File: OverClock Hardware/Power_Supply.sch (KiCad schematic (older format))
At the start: 29 parts, among them J1 USB_C_Plug, U1 AP7365, U2 TLV62569, U3 10M02SCE144

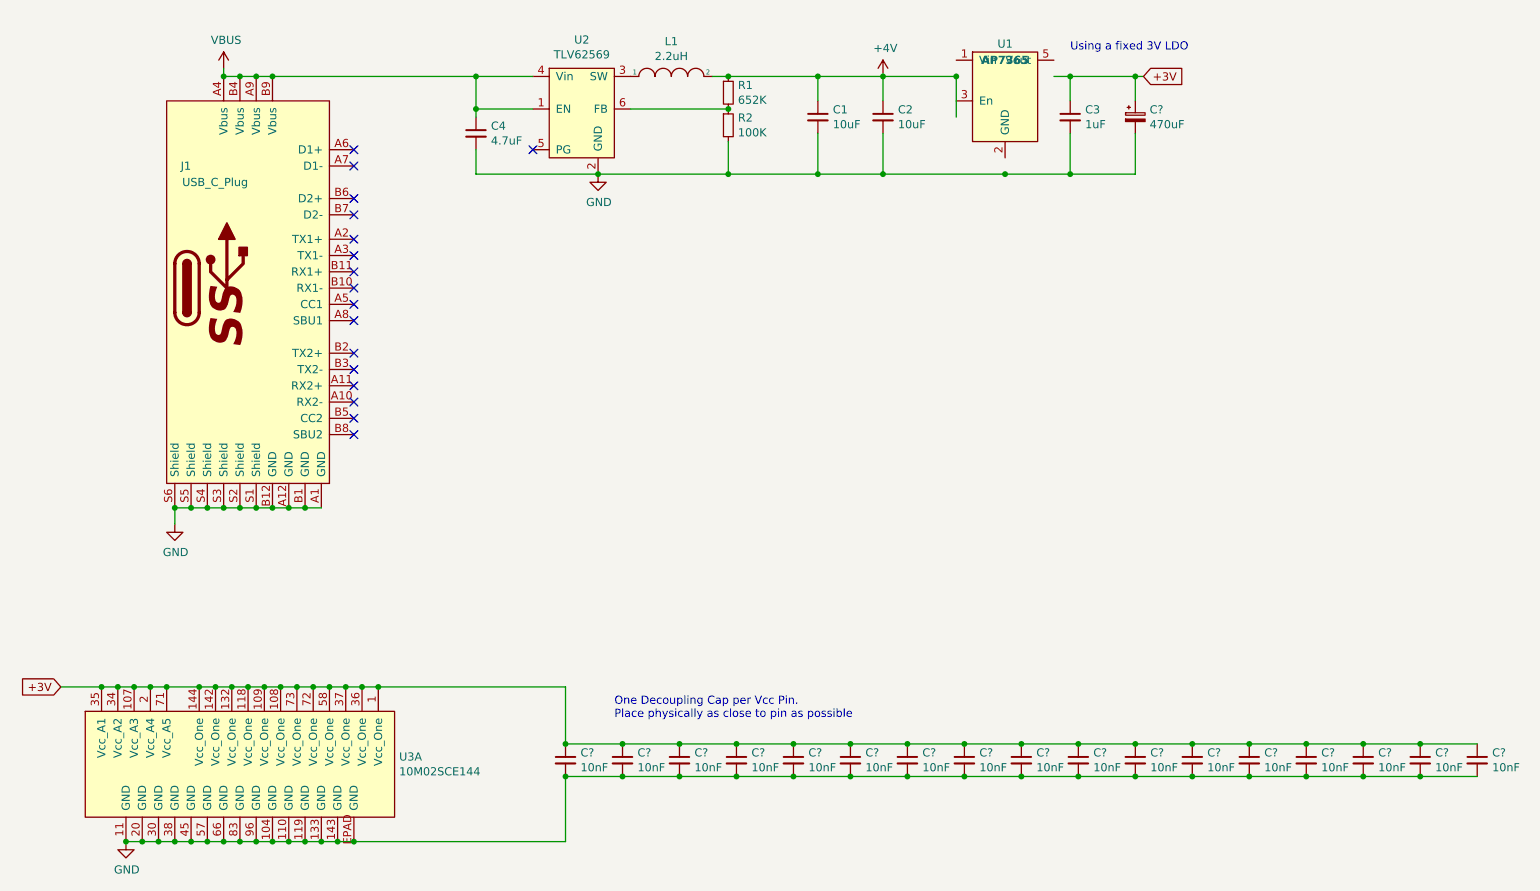
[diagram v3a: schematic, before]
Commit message: Interfaced Hours Digits to FPGA
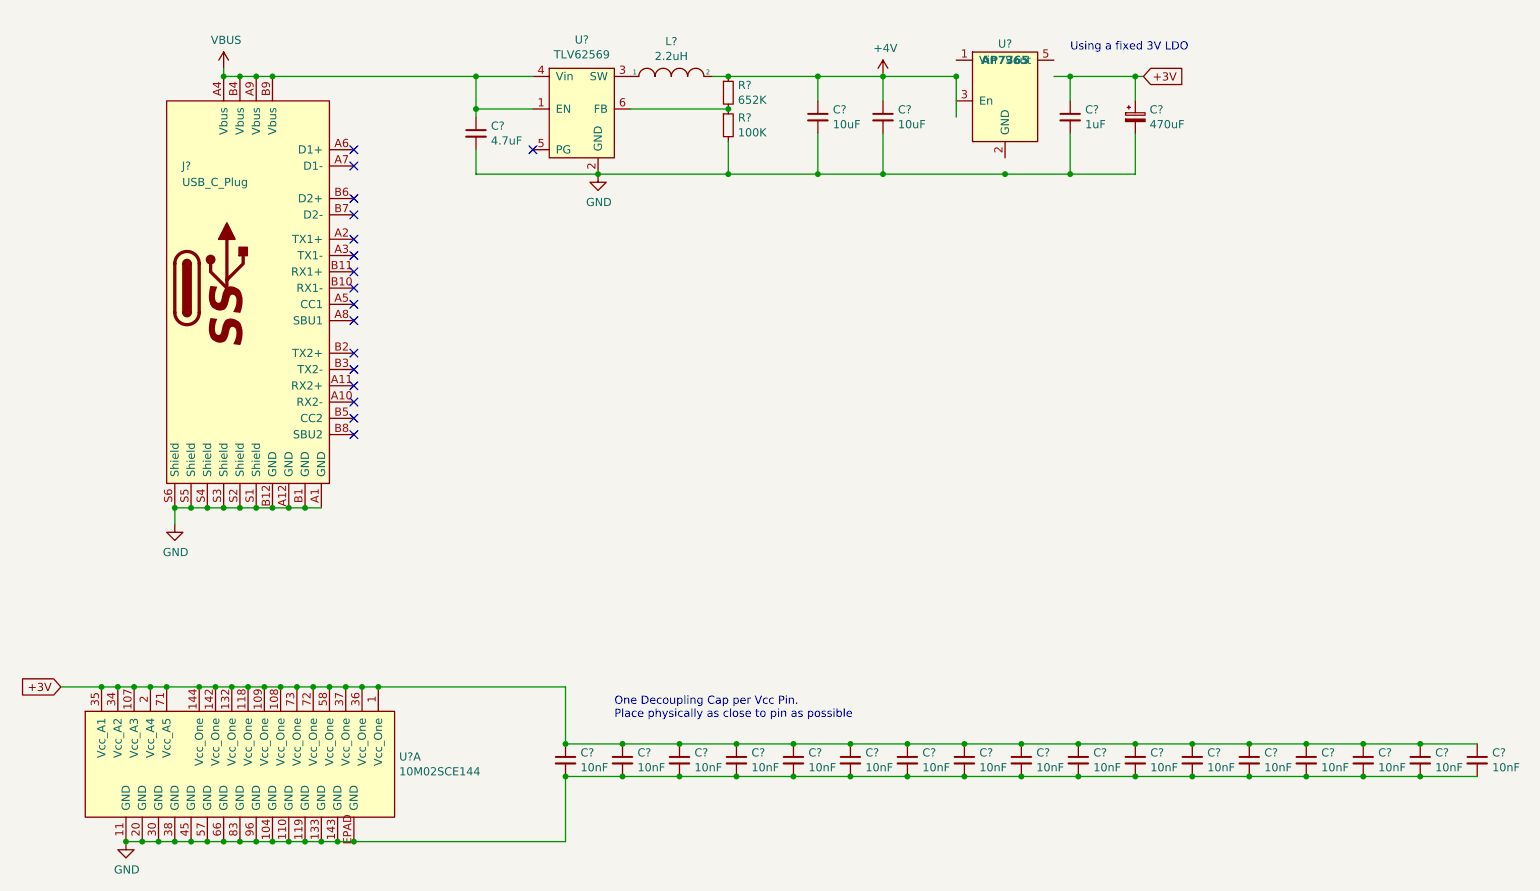
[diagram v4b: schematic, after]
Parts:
- renumbered C1 to C?, C2 to C?, C4 to C?, C3 to C?, J1 to J?, L1 to L?, R1 to R?, R2 to R?, U2 to U?, U1 to U?, U3 to U?
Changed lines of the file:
@@
 $Descr A4 11693 8268
 encoding utf-8
-Sheet 2 3
+Sheet 2 4
 Title ""
 Date ""
@@
 P 1950 2700
 AR Path="/5C666559" Ref="J?"  Part="1"
-AR Path="/5C656C49/5C666559" Ref="J1"  Part="1"
-F 0 "J1" H 1600 3450 50  0000 R CNN
+AR Path="/5C656C49/5C666559" Ref="J?"  Part="1"
+F 0 "J?" H 1600 3450 50  0000 R CNN
 F 1 "USB_C_Plug" H 1950 3350 50  0000 R CNN
 F 2 "Maxted Libs:Hirose_USB_C_Connector" H 2600 3050 50  0001 C CNN
@@
 P 1500 4150
 AR Path="/5C666560" Ref="#PWR?"  Part="1"
-AR Path="/5C656C49/5C666560" Ref="#PWR04"  Part="1"
-F 0 "#PWR04" H 1500 3900 50  0001 C CNN
+AR Path="/5C656C49/5C666560" Ref="#PWR?"  Part="1"
+F 0 "#PWR?" H 1500 3900 50  0001 C CNN
 F 1 "GND" H 1505 3977 50  0000 C CNN
 F 2 "" H 1500 4150 50  0001 C CNN
@@
 P 1800 1350
 AR Path="/5C666579" Ref="#PWR?"  Part="1"
-AR Path="/5C656C49/5C666579" Ref="#PWR01"  Part="1"
-F 0 "#PWR01" H 1800 1200 50  0001 C CNN
+AR Path="/5C656C49/5C666579" Ref="#PWR?"  Part="1"
+F 0 "#PWR?" H 1800 1200 50  0001 C CNN
 F 1 "VBUS" H 1815 1523 50  0000 C CNN
 F 2 "" H 1800 1350 50  0001 C CNN
@@
 P 3950 1650
 AR Path="/5C666597" Ref="U?"  Part="1"
-AR Path="/5C656C49/5C666597" Ref="U2"  Part="1"
-F 0 "U2" H 4000 2125 50  0000 C CNN
+AR Path="/5C656C49/5C666597" Ref="U?"  Part="1"
+F 0 "U?" H 4000 2125 50  0000 C CNN
 F 1 "TLV62569" H 4000 2034 50  0000 C CNN
 F 2 "Maxted Libs:SOT23-6" H 3600 1350 50  0001 C CNN
@@
 P 4100 2000
 AR Path="/5C6665A0" Ref="#PWR?"  Part="1"
-AR Path="/5C656C49/5C6665A0" Ref="#PWR03"  Part="1"
-F 0 "#PWR03" H 4100 1750 50  0001 C CNN
+AR Path="/5C656C49/5C6665A0" Ref="#PWR?"  Part="1"
+F 0 "#PWR?" H 4100 1750 50  0001 C CNN
 F 1 "GND" H 4105 1827 50  0000 C CNN
 F 2 "" H 4100 2000 50  0001 C CNN
@@
 P 4550 1400
 AR Path="/5C6665A7" Ref="L?"  Part="1"
-AR Path="/5C656C49/5C6665A7" Ref="L1"  Part="1"
-F 0 "L1" H 4550 1615 50  0000 C CNN
+AR Path="/5C656C49/5C6665A7" Ref="L?"  Part="1"
+F 0 "L?" H 4550 1615 50  0000 C CNN
 F 1 "2.2uH" H 4550 1524 50  0000 C CNN
 F 2 "Maxted Libs:IHLP3232" H 4550 1400 50  0001 C CNN
@@
 P 4900 1500
 AR Path="/5C6665AE" Ref="R?"  Part="1"
-AR Path="/5C656C49/5C6665AE" Ref="R1"  Part="1"
-F 0 "R1" H 4959 1546 50  0000 L CNN
+AR Path="/5C656C49/5C6665AE" Ref="R?"  Part="1"
+F 0 "R?" H 4959 1546 50  0000 L CNN
 F 1 "652K" H 4959 1455 50  0000 L CNN
 F 2 "Resistor_SMD:R_0805_2012Metric_Pad1.15x1.40mm_HandSolder" H 4900 1500 50  0001 C CNN
@@
 P 4900 1700
 AR Path="/5C6665B5" Ref="R?"  Part="1"
-AR Path="/5C656C49/5C6665B5" Ref="R2"  Part="1"
-F 0 "R2" H 4959 1746 50  0000 L CNN
+AR Path="/5C656C49/5C6665B5" Ref="R?"  Part="1"
+F 0 "R?" H 4959 1746 50  0000 L CNN
 F 1 "100K" H 4959 1655 50  0000 L CNN
 F 2 "Resistor_SMD:R_0805_2012Metric_Pad1.15x1.40mm_HandSolder" H 4900 1700 50  0001 C CNN
@@
 P 5450 1650
 AR Path="/5C6665BF" Ref="C?"  Part="1"
-AR Path="/5C656C49/5C6665BF" Ref="C1"  Part="1"
-F 0 "C1" H 5542 1696 50  0000 L CNN
+AR Path="/5C656C49/5C6665BF" Ref="C?"  Part="1"
+F 0 "C?" H 5542 1696 50  0000 L CNN
 F 1 "10uF" H 5542 1605 50  0000 L CNN
 F 2 "Capacitor_SMD:C_0805_2012Metric_Pad1.15x1.40mm_HandSolder" H 5450 1650 50  0001 C CNN
@@
 P 5850 1650
 AR Path="/5C6665C6" Ref="C?"  Part="1"
-AR Path="/5C656C49/5C6665C6" Ref="C2"  Part="1"
-F 0 "C2" H 5942 1696 50  0000 L CNN
+AR Path="/5C656C49/5C6665C6" Ref="C?"  Part="1"
+F 0 "C?" H 5942 1696 50  0000 L CNN
 F 1 "10uF" H 5942 1605 50  0000 L CNN
 F 2 "Capacitor_SMD:C_0805_2012Metric_Pad1.15x1.40mm_HandSolder" H 5850 1650 50  0001 C CNN
@@
 P 3350 1750
 AR Path="/5C6665DC" Ref="C?"  Part="1"
-AR Path="/5C656C49/5C6665DC" Ref="C4"  Part="1"
-F 0 "C4" H 3442 1796 50  0000 L CNN
+AR Path="/5C656C49/5C6665DC" Ref="C?"  Part="1"
+F 0 "C?" H 3442 1796 50  0000 L CNN
 F 1 "4.7uF" H 3442 1705 50  0000 L CNN
 F 2 "Capacitor_SMD:C_0805_2012Metric_Pad1.15x1.40mm_HandSolder" H 3350 1750 50  0001 C CNN
@@
 P 5850 1400
 AR Path="/5C6665EC" Ref="#PWR?"  Part="1"
-AR Path="/5C656C49/5C6665EC" Ref="#PWR02"  Part="1"
-F 0 "#PWR02" H 5850 1250 50  0001 C CNN
+AR Path="/5C656C49/5C6665EC" Ref="#PWR?"  Part="1"
+F 0 "#PWR?" H 5850 1250 50  0001 C CNN
 F 1 "+4V" H 5865 1573 50  0000 C CNN
 F 2 "" H 5850 1400 50  0001 C CNN
@@
 P 6600 1500
 AR Path="/5C6665F4" Ref="U?"  Part="1"
-AR Path="/5C656C49/5C6665F4" Ref="U1"  Part="1"
-F 0 "U1" H 6600 1800 50  0000 C CNN
+AR Path="/5C656C49/5C6665F4" Ref="U?"  Part="1"
+F 0 "U?" H 6600 1800 50  0000 C CNN
 F 1 "AP7365" H 6600 1700 50  0000 C CNB
 F 2 "Maxted Libs:SOT-23-5" H 6600 950 50  0001 C CNN
@@
 P 7000 1650
 AR Path="/5C666601" Ref="C?"  Part="1"
-AR Path="/5C656C49/5C666601" Ref="C3"  Part="1"
-F 0 "C3" H 7092 1696 50  0000 L CNN
+AR Path="/5C656C49/5C666601" Ref="C?"  Part="1"
+F 0 "C?" H 7092 1696 50  0000 L CNN
 F 1 "1uF" H 7092 1605 50  0000 L CNN
 F 2 "Capacitor_SMD:C_0805_2012Metric_Pad1.15x1.40mm_HandSolder" H 7000 1650 50  0001 C CNN
@@
 Connection ~ 7000 1400
 $Comp
-L Maxted_Libs:10M02SCE144 U3
+L Maxted_Libs:10M02SCE144 U?
 U 1 1 5C66E890
 P 1900 5700
-F 0 "U3" H 2878 5821 50  0000 L CNN
+F 0 "U?" H 2878 5821 50  0000 L CNN
 F 1 "10M02SCE144" H 2878 5730 50  0000 L CNN
 F 2 "Maxted Libs:QFP-144_EPAD_20x20_Pitch0.5mm" H 2900 6500 50  0001 C CNN
@@
 $EndComp
 $Comp
-L power:GND #PWR05
+L power:GND #PWR?
 U 1 1 5C66E982
 P 1200 6100
-F 0 "#PWR05" H 1200 5850 50  0001 C CNN
+F 0 "#PWR?" H 1200 5850 50  0001 C CNN
 F 1 "GND" H 1205 5927 50  0000 C CNN
 F 2 "" H 1200 6100 50  0001 C CNN

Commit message: Completed Schematic and ran ERC
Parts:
- gave numbers to parts that had none: 29

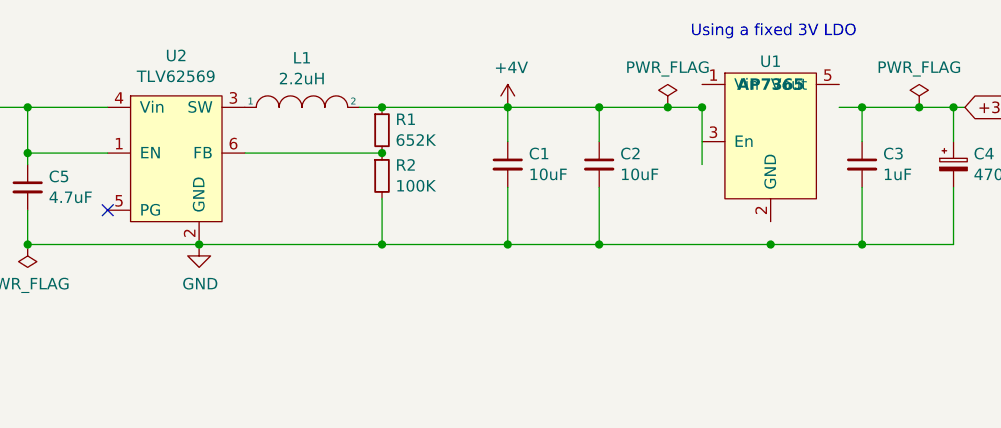
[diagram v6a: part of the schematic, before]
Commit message: Matched symbols to footprints and generated netlist
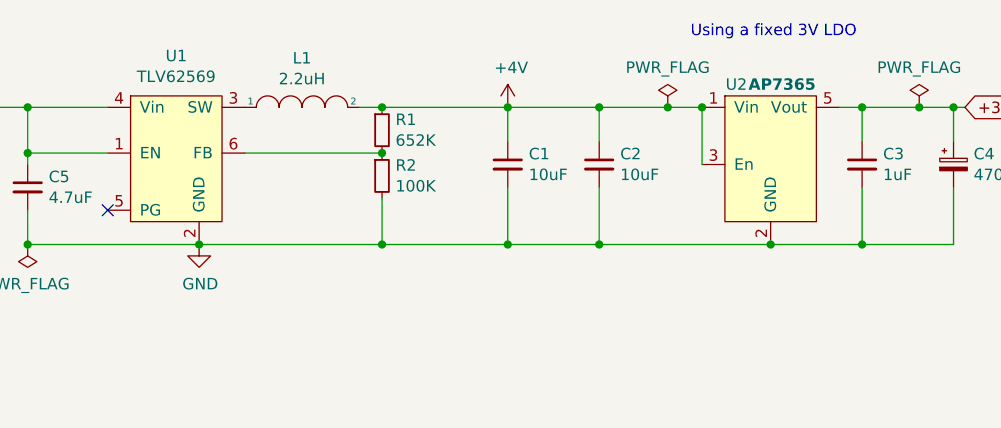
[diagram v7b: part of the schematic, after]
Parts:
- renumbered U2 to U1, U1 to U2
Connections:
- net +3V: now also U2.5 (Vout)
- net +4V: now also U2.1 (Vin), U2.3 (En)
- net GND: now also U2.2 (GND)
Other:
- moved on the sheet: U2
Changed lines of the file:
@@
 P 3950 1650
 AR Path="/5C666597" Ref="U?"  Part="1"
-AR Path="/5C656C49/5C666597" Ref="U2"  Part="1"
-F 0 "U2" H 4000 2125 50  0000 C CNN
+AR Path="/5C656C49/5C666597" Ref="U1"  Part="1"
+F 0 "U1" H 4000 2125 50  0000 C CNN
 F 1 "TLV62569" H 4000 2034 50  0000 C CNN
 F 2 "Maxted Libs:SOT23-6" H 3600 1350 50  0001 C CNN
@@
 L Maxted_Libs:AP7365 U?
 U 1 1 5C6665F4
-P 6600 1500
+P 6600 1600
 AR Path="/5C6665F4" Ref="U?"  Part="1"
-AR Path="/5C656C49/5C6665F4" Ref="U1"  Part="1"
-F 0 "U1" H 6600 1800 50  0000 C CNN
-F 1 "AP7365" H 6600 1700 50  0000 C CNB
-F 2 "Maxted Libs:SOT-23-5" H 6600 950 50  0001 C CNN
-F 3 "https://www.diodes.com/assets/Datasheets/AP7365.pdf" H 6650 850 50  0001 C CNN
-F 4 "https://www.digikey.co.nz/product-detail/en/diodes-incorporated/AP7365-WG-7/AP7365-WG-7DICT-ND/4505315" H 6600 1500 50  0001 C CNN "Supplier"
-	1    6600 1500
+AR Path="/5C656C49/5C6665F4" Ref="U2"  Part="1"
+F 0 "U2" H 6450 1900 50  0000 C CNN
+F 1 "AP7365" H 6650 1900 50  0000 C CNB
+F 2 "Maxted Libs:SOT-23-5" H 6600 1050 50  0001 C CNN
+F 3 "https://www.diodes.com/assets/Datasheets/AP7365.pdf" H 6650 950 50  0001 C CNN
+F 4 "https://www.digikey.co.nz/product-detail/en/diodes-incorporated/AP7365-WG-7/AP7365-WG-7DICT-ND/4505315" H 6600 1600 50  0001 C CNN "Supplier"
+	1    6600 1600
 	1    0    0    -1
 $EndComp

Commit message: Started to route out basic blocks
- FPGA Decoupling Caps
- 2 of the digit MOSFETS
- Power supply
- FPGA location
- Digit locations
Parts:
- C10, C11, C12, C13, C14, C15, C16, C17, C18, C19, C20, C21, C22, C6, C7, C8, C9: footprint Capacitor_SMD:C_0603_1608Metric_Pad1.05x0.95mm_HandSolder -> Capacitor_SMD:C_0805_2012Metric_Pad1.15x1.40mm_HandSolder
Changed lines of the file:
@@
 F 0 "C6" H 3992 5646 50  0000 L CNN
 F 1 "10nF" H 3992 5555 50  0000 L CNN
-F 2 "Capacitor_SMD:C_0603_1608Metric_Pad1.05x0.95mm_HandSolder" H 3900 5600 50  0001 C CNN
+F 2 "Capacitor_SMD:C_0805_2012Metric_Pad1.15x1.40mm_HandSolder" H 3900 5600 50  0001 C CNN
 F 3 "~" H 3900 5600 50  0001 C CNN
 	1    3900 5600
@@
 F 0 "C7" H 4342 5646 50  0000 L CNN
 F 1 "10nF" H 4342 5555 50  0000 L CNN
-F 2 "Capacitor_SMD:C_0603_1608Metric_Pad1.05x0.95mm_HandSolder" H 4250 5600 50  0001 C CNN
+F 2 "Capacitor_SMD:C_0805_2012Metric_Pad1.15x1.40mm_HandSolder" H 4250 5600 50  0001 C CNN
 F 3 "~" H 4250 5600 50  0001 C CNN
 	1    4250 5600
@@
 F 0 "C8" H 4692 5646 50  0000 L CNN
 F 1 "10nF" H 4692 5555 50  0000 L CNN
-F 2 "Capacitor_SMD:C_0603_1608Metric_Pad1.05x0.95mm_HandSolder" H 4600 5600 50  0001 C CNN
+F 2 "Capacitor_SMD:C_0805_2012Metric_Pad1.15x1.40mm_HandSolder" H 4600 5600 50  0001 C CNN
 F 3 "~" H 4600 5600 50  0001 C CNN
 	1    4600 5600
@@
 F 0 "C9" H 5042 5646 50  0000 L CNN
 F 1 "10nF" H 5042 5555 50  0000 L CNN
-F 2 "Capacitor_SMD:C_0603_1608Metric_Pad1.05x0.95mm_HandSolder" H 4950 5600 50  0001 C CNN
+F 2 "Capacitor_SMD:C_0805_2012Metric_Pad1.15x1.40mm_HandSolder" H 4950 5600 50  0001 C CNN
 F 3 "~" H 4950 5600 50  0001 C CNN
 	1    4950 5600
@@
 F 0 "C10" H 5392 5646 50  0000 L CNN
 F 1 "10nF" H 5392 5555 50  0000 L CNN
-F 2 "Capacitor_SMD:C_0603_1608Metric_Pad1.05x0.95mm_HandSolder" H 5300 5600 50  0001 C CNN
+F 2 "Capacitor_SMD:C_0805_2012Metric_Pad1.15x1.40mm_HandSolder" H 5300 5600 50  0001 C CNN
 F 3 "~" H 5300 5600 50  0001 C CNN
 	1    5300 5600
@@
 F 0 "C11" H 5742 5646 50  0000 L CNN
 F 1 "10nF" H 5742 5555 50  0000 L CNN
-F 2 "Capacitor_SMD:C_0603_1608Metric_Pad1.05x0.95mm_HandSolder" H 5650 5600 50  0001 C CNN
+F 2 "Capacitor_SMD:C_0805_2012Metric_Pad1.15x1.40mm_HandSolder" H 5650 5600 50  0001 C CNN
 F 3 "~" H 5650 5600 50  0001 C CNN
 	1    5650 5600
@@
 F 0 "C12" H 6092 5646 50  0000 L CNN
 F 1 "10nF" H 6092 5555 50  0000 L CNN
-F 2 "Capacitor_SMD:C_0603_1608Metric_Pad1.05x0.95mm_HandSolder" H 6000 5600 50  0001 C CNN
+F 2 "Capacitor_SMD:C_0805_2012Metric_Pad1.15x1.40mm_HandSolder" H 6000 5600 50  0001 C CNN
 F 3 "~" H 6000 5600 50  0001 C CNN
 	1    6000 5600
@@
 F 0 "C13" H 6442 5646 50  0000 L CNN
 F 1 "10nF" H 6442 5555 50  0000 L CNN
-F 2 "Capacitor_SMD:C_0603_1608Metric_Pad1.05x0.95mm_HandSolder" H 6350 5600 50  0001 C CNN
+F 2 "Capacitor_SMD:C_0805_2012Metric_Pad1.15x1.40mm_HandSolder" H 6350 5600 50  0001 C CNN
 F 3 "~" H 6350 5600 50  0001 C CNN
 	1    6350 5600
@@
 F 0 "C14" H 6792 5646 50  0000 L CNN
 F 1 "10nF" H 6792 5555 50  0000 L CNN
-F 2 "Capacitor_SMD:C_0603_1608Metric_Pad1.05x0.95mm_HandSolder" H 6700 5600 50  0001 C CNN
+F 2 "Capacitor_SMD:C_0805_2012Metric_Pad1.15x1.40mm_HandSolder" H 6700 5600 50  0001 C CNN
 F 3 "~" H 6700 5600 50  0001 C CNN
 	1    6700 5600
@@
 F 0 "C15" H 7142 5646 50  0000 L CNN
 F 1 "10nF" H 7142 5555 50  0000 L CNN
-F 2 "Capacitor_SMD:C_0603_1608Metric_Pad1.05x0.95mm_HandSolder" H 7050 5600 50  0001 C CNN
+F 2 "Capacitor_SMD:C_0805_2012Metric_Pad1.15x1.40mm_HandSolder" H 7050 5600 50  0001 C CNN
 F 3 "~" H 7050 5600 50  0001 C CNN
 	1    7050 5600
@@
 F 0 "C16" H 7492 5646 50  0000 L CNN
 F 1 "10nF" H 7492 5555 50  0000 L CNN
-F 2 "Capacitor_SMD:C_0603_1608Metric_Pad1.05x0.95mm_HandSolder" H 7400 5600 50  0001 C CNN
+F 2 "Capacitor_SMD:C_0805_2012Metric_Pad1.15x1.40mm_HandSolder" H 7400 5600 50  0001 C CNN
 F 3 "~" H 7400 5600 50  0001 C CNN
 	1    7400 5600
@@
 F 0 "C17" H 7842 5646 50  0000 L CNN
 F 1 "10nF" H 7842 5555 50  0000 L CNN
-F 2 "Capacitor_SMD:C_0603_1608Metric_Pad1.05x0.95mm_HandSolder" H 7750 5600 50  0001 C CNN
+F 2 "Capacitor_SMD:C_0805_2012Metric_Pad1.15x1.40mm_HandSolder" H 7750 5600 50  0001 C CNN
 F 3 "~" H 7750 5600 50  0001 C CNN
 	1    7750 5600
@@
 F 0 "C18" H 8192 5646 50  0000 L CNN
 F 1 "10nF" H 8192 5555 50  0000 L CNN
-F 2 "Capacitor_SMD:C_0603_1608Metric_Pad1.05x0.95mm_HandSolder" H 8100 5600 50  0001 C CNN
+F 2 "Capacitor_SMD:C_0805_2012Metric_Pad1.15x1.40mm_HandSolder" H 8100 5600 50  0001 C CNN
 F 3 "~" H 8100 5600 50  0001 C CNN
 	1    8100 5600
@@
 F 0 "C19" H 8542 5646 50  0000 L CNN
 F 1 "10nF" H 8542 5555 50  0000 L CNN
-F 2 "Capacitor_SMD:C_0603_1608Metric_Pad1.05x0.95mm_HandSolder" H 8450 5600 50  0001 C CNN
+F 2 "Capacitor_SMD:C_0805_2012Metric_Pad1.15x1.40mm_HandSolder" H 8450 5600 50  0001 C CNN
 F 3 "~" H 8450 5600 50  0001 C CNN
 	1    8450 5600
@@
 F 0 "C20" H 8892 5646 50  0000 L CNN
 F 1 "10nF" H 8892 5555 50  0000 L CNN
-F 2 "Capacitor_SMD:C_0603_1608Metric_Pad1.05x0.95mm_HandSolder" H 8800 5600 50  0001 C CNN
+F 2 "Capacitor_SMD:C_0805_2012Metric_Pad1.15x1.40mm_HandSolder" H 8800 5600 50  0001 C CNN
 F 3 "~" H 8800 5600 50  0001 C CNN
 	1    8800 5600
@@
 F 0 "C21" H 9242 5646 50  0000 L CNN
 F 1 "10nF" H 9242 5555 50  0000 L CNN
-F 2 "Capacitor_SMD:C_0603_1608Metric_Pad1.05x0.95mm_HandSolder" H 9150 5600 50  0001 C CNN
+F 2 "Capacitor_SMD:C_0805_2012Metric_Pad1.15x1.40mm_HandSolder" H 9150 5600 50  0001 C CNN
 F 3 "~" H 9150 5600 50  0001 C CNN
 	1    9150 5600
@@
 F 0 "C22" H 9592 5646 50  0000 L CNN
 F 1 "10nF" H 9592 5555 50  0000 L CNN
-F 2 "Capacitor_SMD:C_0603_1608Metric_Pad1.05x0.95mm_HandSolder" H 9500 5600 50  0001 C CNN
+F 2 "Capacitor_SMD:C_0805_2012Metric_Pad1.15x1.40mm_HandSolder" H 9500 5600 50  0001 C CNN
 F 3 "~" H 9500 5600 50  0001 C CNN
 	1    9500 5600
